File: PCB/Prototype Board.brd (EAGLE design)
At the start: 55.9 x 76.2 mm, 78 parts, among them IC1 SMF05CT1G, J1 USB Type C, Q1 S8050, Q10 20V/0.2A/8MHz/1.2Ω/1Vth, Q2 20V/0.2A/8MHz/1.2Ω/1Vth, Q3 20V/4.2A/52mΩ/1.4W, Q4 S8050, Q5 20V/0.2A/8MHz/1.2Ω/1Vth, Q6 20V/0.2A/8MHz/1.2Ω/1Vth, Q7 20V/0.2A/8MHz/1.2Ω/1Vth, Q8 20V/0.2A/8MHz/1.2Ω/1Vth, U1 9DoF IMU, U2 MCP73831, U3 ESP-WROOM-32, U5 DWM1000, U7 CH340C

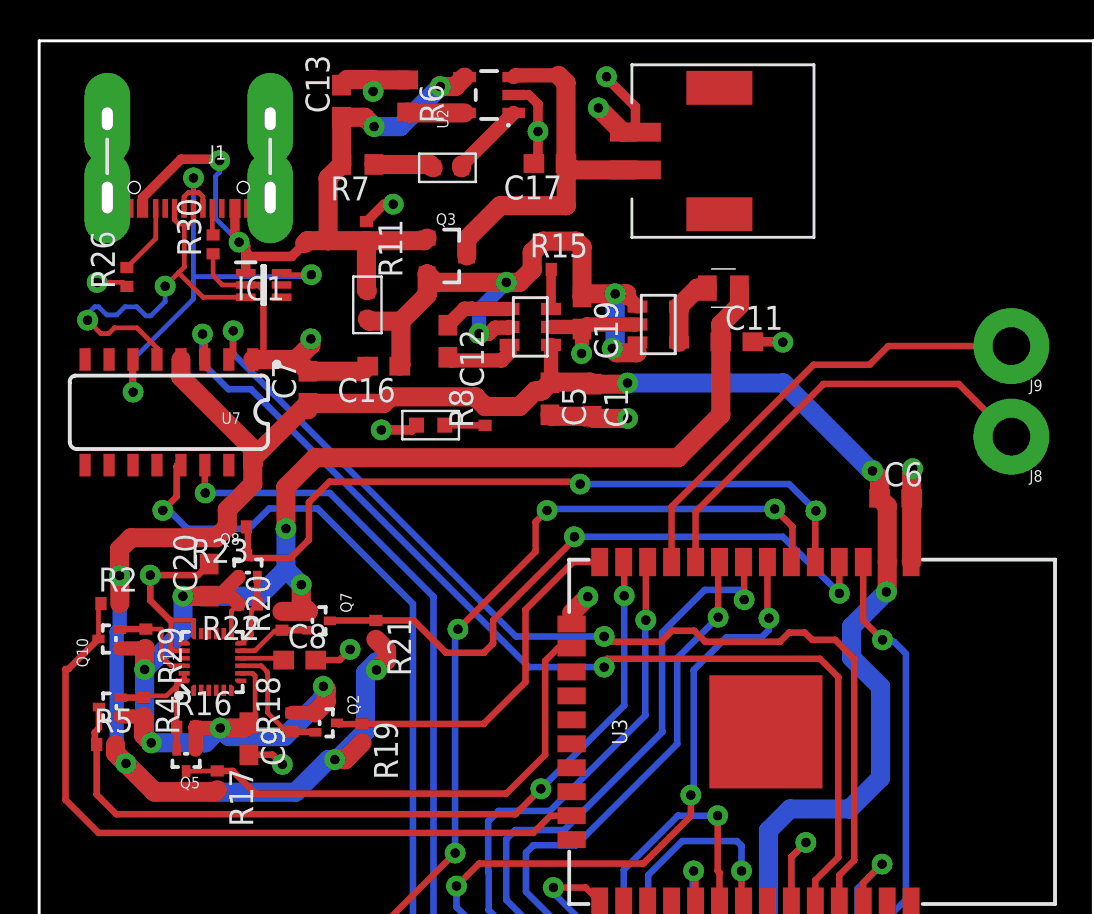
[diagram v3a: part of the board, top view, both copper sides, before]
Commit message: Resolved all DRC violations
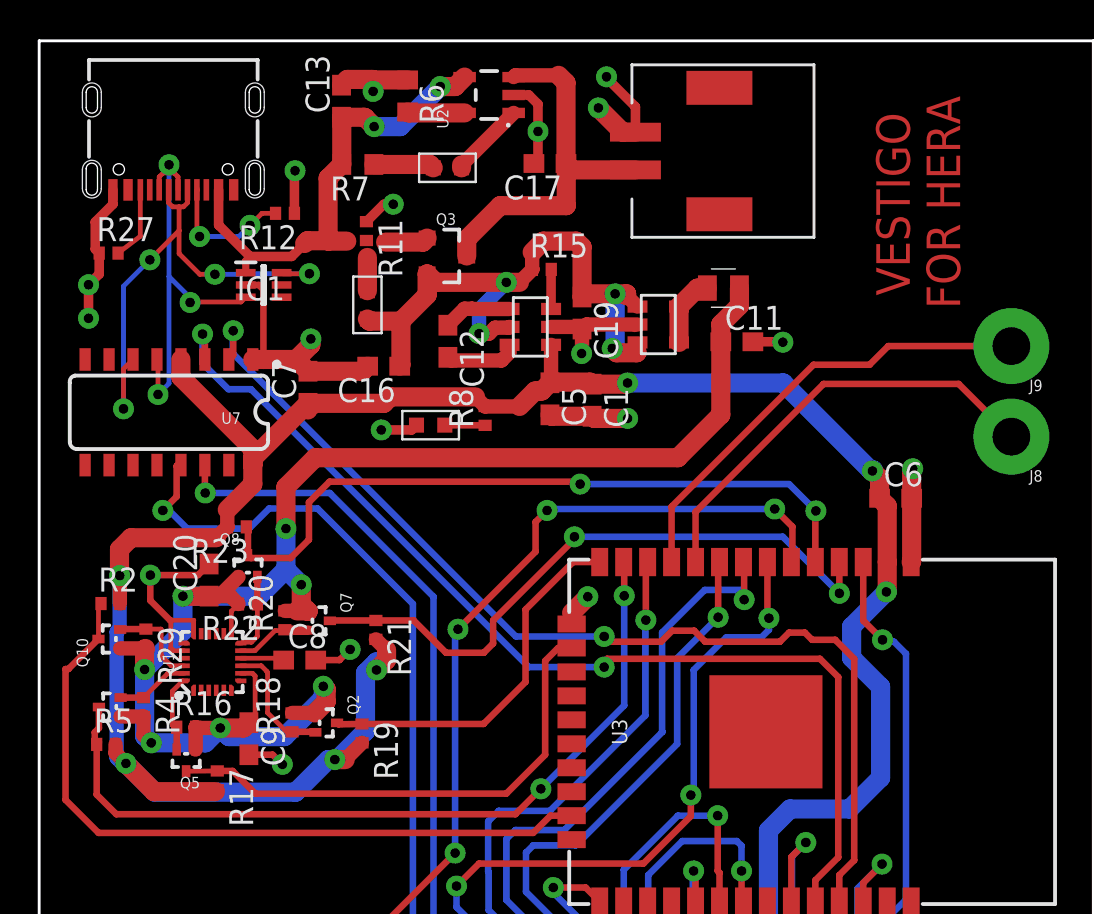
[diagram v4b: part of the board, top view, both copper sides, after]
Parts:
- removed J1: USB Type C, SparkFun-Connectors:USB-C-16P-2LAYER-PADS
- removed R26, R30: R_5.1K_0402, JLC PCB Basic Parts_loc:R0402
- added R12, R27: R_5.1K_0402, JLC PCB Basic Parts_loc:R0402
- added U$10: USBC19, customlib:USBC19
- moved R20 0.15 mm to (13.0, 45.5)
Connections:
- removed net N$5: J1.B5, R26.2
- removed net N$6: J1.A5, R30.2
- new net N$16: R27.2, U$10.B5
- new net N$17: R12.2, U$10.A5
- net D_N: now also U$10.A7, U$10.B7; no longer J1.A7, J1.B7
- net D_P: now also U$10.A6, U$10.B6; no longer J1.A6, J1.B6
- net GND: now also R12.1, R27.1, U$10.A12; no longer J1.GND, J1.GND2, J1.SHLD1, J1.SHLD2, J1.SHLD3, J1.SHLD4, R26.1, R30.1
- net V_USB: now also U$10.A4; no longer J1.VBUS1, J1.VBUS2
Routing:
- net V_USB: track 42.0 -> 29.4 mm, vias 4 -> 2
- net N$17: track 0.00 -> 7.18 mm, vias 0 -> 2
- net N$16: track 0.00 -> 3.94 mm
- net N$5: track 3.77 -> 0.00 mm
- net GND: track 126.1 -> 128.2 mm, vias 23 -> 25
- net D_N: track 25.5 -> 27.4 mm, vias 3 -> 4
- net N$6: track 1.42 -> 0.00 mm
- net D_P: track 21.7 -> 22.2 mm, vias 2 -> 3
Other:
- board text added: "VESTIGO FOR HERA"

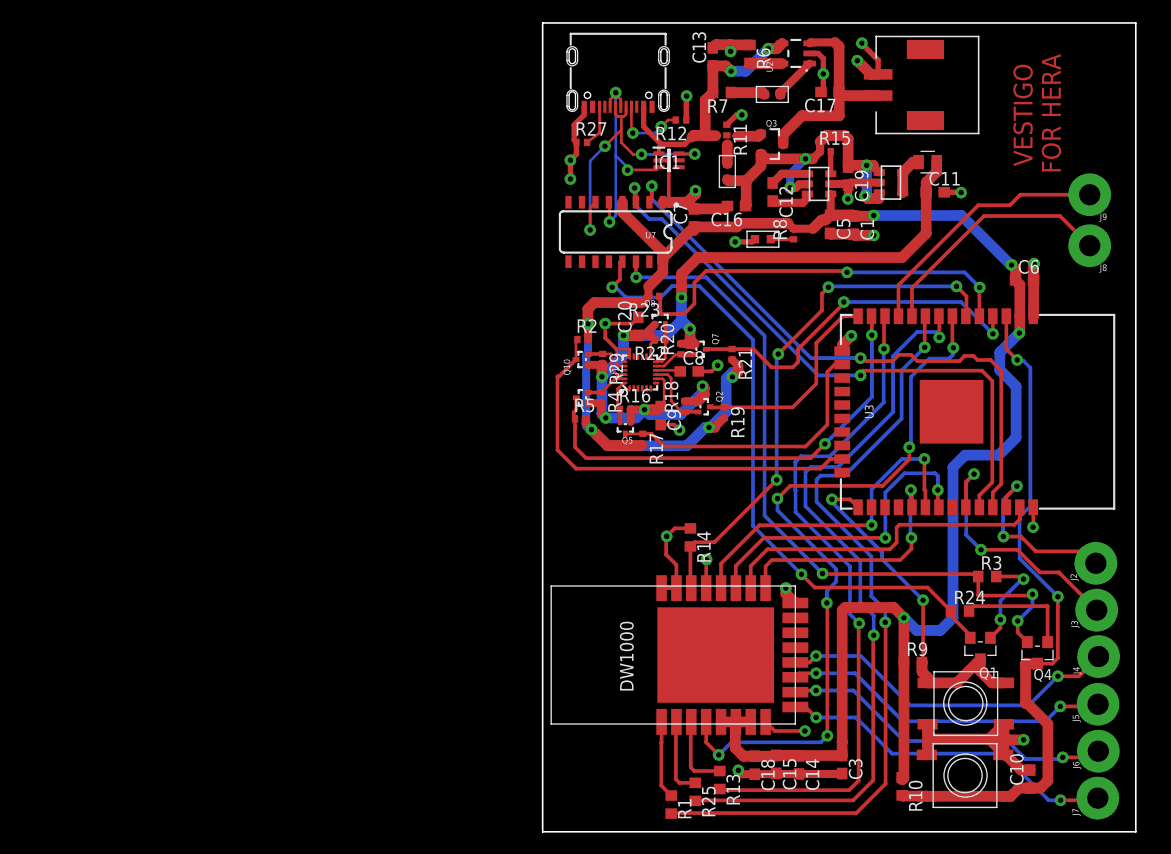
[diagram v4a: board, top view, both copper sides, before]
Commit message: Completed First Draft of PCB + Assembly Details
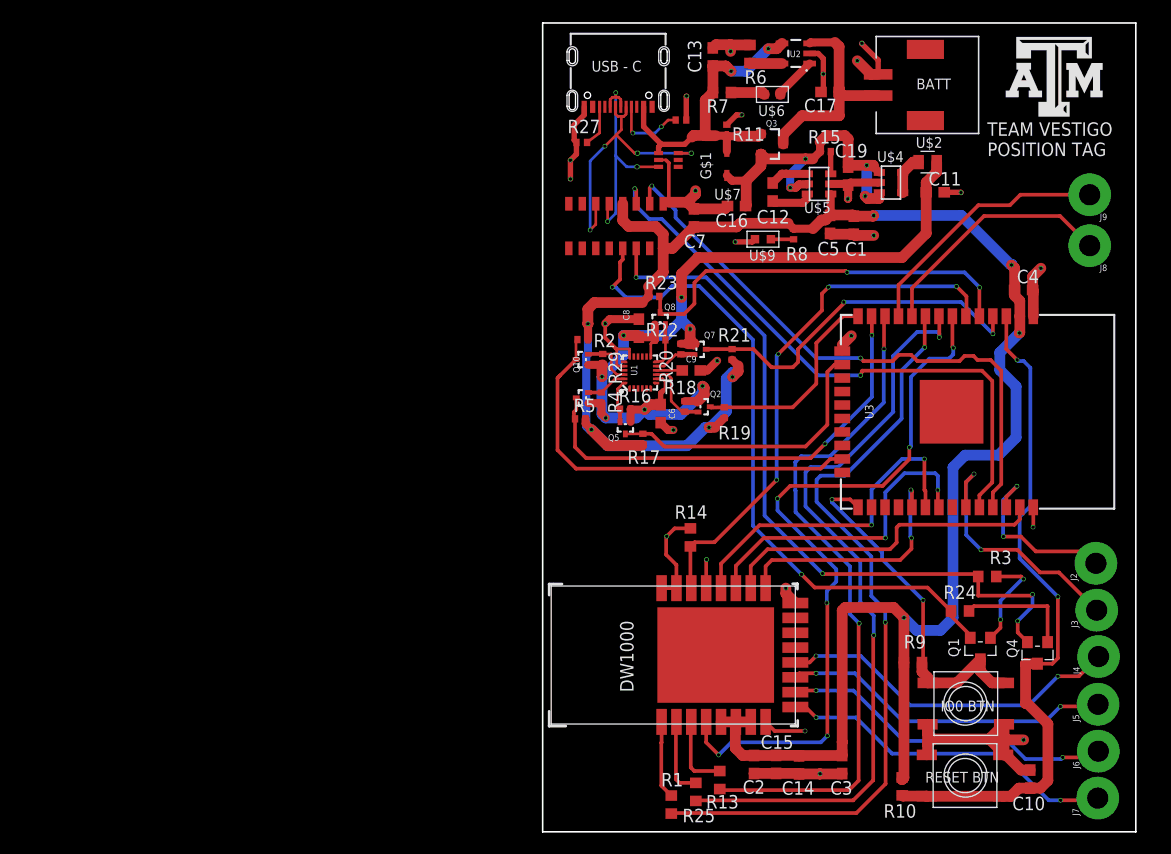
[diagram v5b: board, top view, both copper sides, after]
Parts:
- removed C18: C_10UF/25V_0603, JLC PCB Basic Parts_loc:C0603
- removed C20: C_100NF/50V_0603, JLC PCB Basic Parts_loc:C0603
- removed IC1: SMF05CT1G, SMF05CT1G:SOT65P210X110-6N
- removed U7: CH340C, SparkFun-IC-Comms:SO016
- added C2, C4: C_10UF/10V_0603, JLC PCB Basic Parts_loc:C0603
- added D1: BAT60AE6327HTSA1, BAT60AE6327HTSA1:SOD2513X110N
- added U$11: CH340B, customlib:SOP-16
- C6: value C_10UF/25V_0603 -> 1.0uF; device JLC PCB Basic Parts_loc:C0603 -> SparkFun-Capacitors:0603
- C8: value C_100NF/50V_0603 -> 0.1uF; device JLC PCB Basic Parts_loc:C0603 -> SparkFun-Capacitors:0603
- C9: value C_1UF/50V_0603 -> 0.1uF; device JLC PCB Basic Parts_loc:C0603 -> SparkFun-Capacitors:0603
- U$7: value 19-217/GHC-YR1S2/3T -> TPSMF05CT1G; device customlib:19-217/GHC-YR1S2/3T -> customlib:TPSMF05CT1G
- moved C6 36.5 mm to (11.1, 39.4), turned to 270 degrees
- moved C8 6.25 mm to (9.06, 47.4), turned to 90 degrees
- moved U$7 5.66 mm to (11.8, 63.3)
- moved C9 5.14 mm to (14.0, 43.5), turned to 0 degrees
- moved R25 0.05 mm to (14.4, 3.76)
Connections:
- net 1.8V: now also C6.1, C8.1; no longer C20.1, C9.1
- net 3.3V: now also C2.1, C4.1, U$11.16, U$11.4; no longer C18.1, C6.1, U7.16, U7.4
- net DTR: now also U$11.13; no longer U7.13
- net D_N: now also U$11.6, U$7.6; no longer IC1.6, U7.6
- net D_P: now also U$11.5, U$7.3; no longer IC1.3, U7.5
- net GND: now also C2.2, C4.2, U$11.1, U$7.2; no longer C18.2, C20.2, IC1.2, U7.1
- net N$13: now also C9.1; no longer C8.1
- net RTS: now also U$11.14; no longer U7.14
- net RX-TX_N: now also U$11.2; no longer U7.2
- net RX-TX_P: now also U$11.3; no longer U7.3
- net V_IN: now also D1.1; no longer U$7.2
- net V_USB: now also D1.2; no longer IC1.1
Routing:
- net GND: track 128.2 -> 126.2 mm
- net V_USB: track 29.4 -> 31.2 mm
- net RTS: track 67.8 -> 69.0 mm
- net D_N: track 27.4 -> 26.2 mm
- net DTR: track 62.1 -> 63.2 mm
- net 1.8V: track 88.6 -> 88.0 mm
- net D_P: track 22.2 -> 21.6 mm
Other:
- board text added: "BATT"
- board text added: "G$1"
- board text added: "IO0 BTN"
- board text added: "RESET BTN"
- board text added: "TEAM VESTIGO POSITION TAG"
- board text added: "U$2"
- board text added: "U$4"
- board text added: "U$5"
- board text added: "U$6"
- board text added: "U$7"
- board text added: "U$9"
- board text added: "USB - C"
- board text removed: "VESTIGO FOR HERA"

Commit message: Finalized PCB
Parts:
- removed U1: 9DoF IMU, SparkFun-Sensors:QFN24-3X3
- added U$12: ICM20948, customlib:ICM20948
- moved U$6 0.43 mm to (21.3, 69.7), turned to 180 degrees
- moved U$9 0.13 mm to (20.8, 55.7), turned to 0 degrees
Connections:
- net 1.8V: now also U$12.13, U$12.8; no longer U1.13, U1.8
- net CHG_LED: now also U$6.2; no longer U$6.1
- net FSYNC/IO36: now also U$12.11; no longer U1.11
- net GND: now also U$12.18, U$12.20, U$9.1, U3.GND; no longer U$9.2, U1.18, U1.20
- net GPIO12/SDO: now also U$12.9; no longer U1.9
- net GPIO13/SDI: now also U$12.24; no longer U1.24
- net GPIO14/SCLK: now also U$12.23; no longer U1.23
- net GPIO15/CS: now also U$12.22; no longer U1.22
- net INT/IO39: now also U$12.12; no longer U1.12
- net N$13: now also U$12.10; no longer U1.10
- net N$4: now also U$9.2; no longer U$9.1
- net N$7: now also U$6.1; no longer U$6.2
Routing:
- net GND: track 126.2 -> 194.7 mm, vias 25 -> 60
- net N$7: track 4.05 -> 4.87 mm
